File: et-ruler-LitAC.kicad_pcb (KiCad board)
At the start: 2 copper layers, 166 x 28 mm, 27 parts, among them J1 Conn_01x03, J2 AudioJack2, J3 Pmod-Interface-GPIO6, J4 Pmod-Interface-GPIO6, SW1 SW_DPDT, U1 OP07

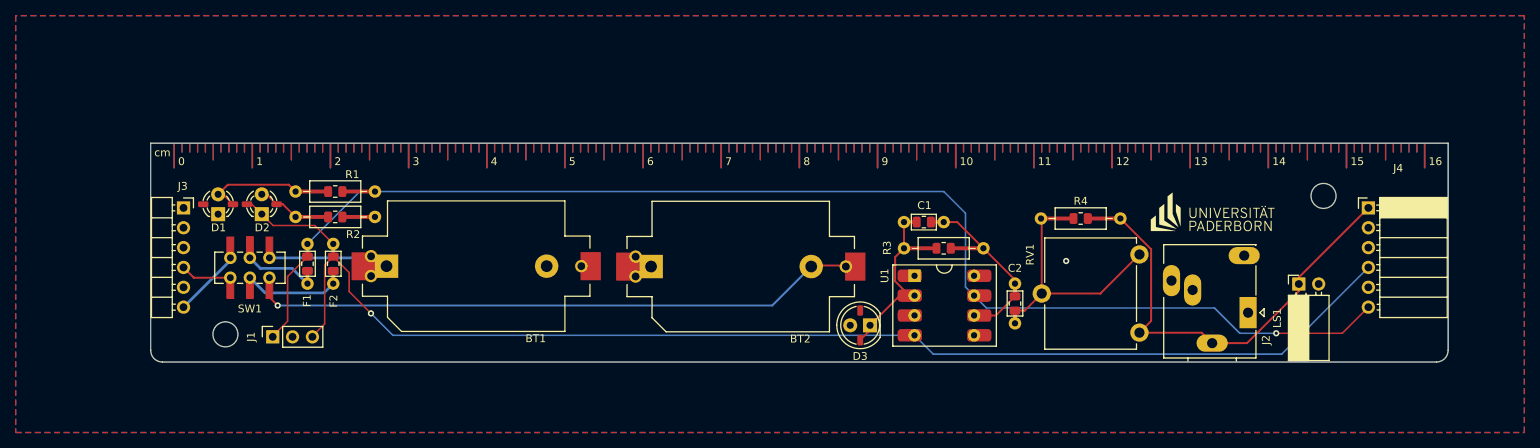
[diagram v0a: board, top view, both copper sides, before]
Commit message: Widen power tracks
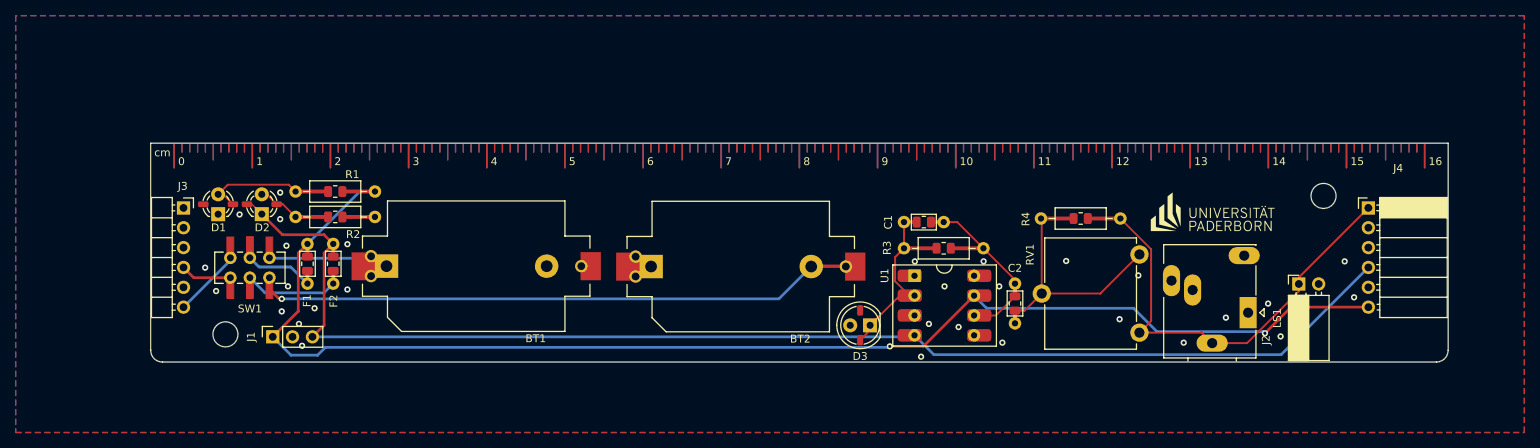
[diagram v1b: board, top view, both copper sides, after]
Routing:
- net V+: track 165.1 -> 175.4 mm, vias 1 -> 2
- net Net-(BT2--): track 78.0 -> 81.1 mm
- net Net-(BT1-+): track 14.6 -> 17.3 mm
- net V-: track 168.2 -> 169.3 mm, vias 1 -> 0
- net GND: vias 1 -> 30

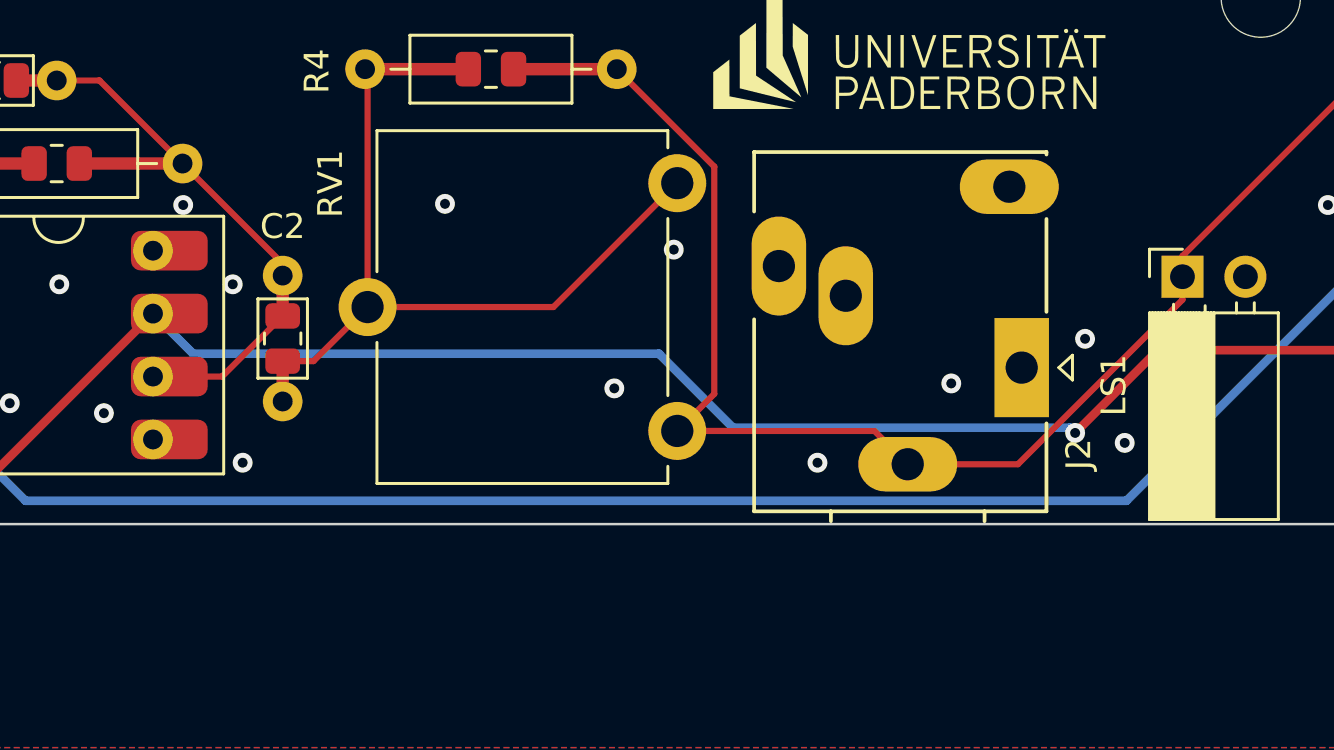
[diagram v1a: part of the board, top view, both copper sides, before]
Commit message: Use correct audio jack
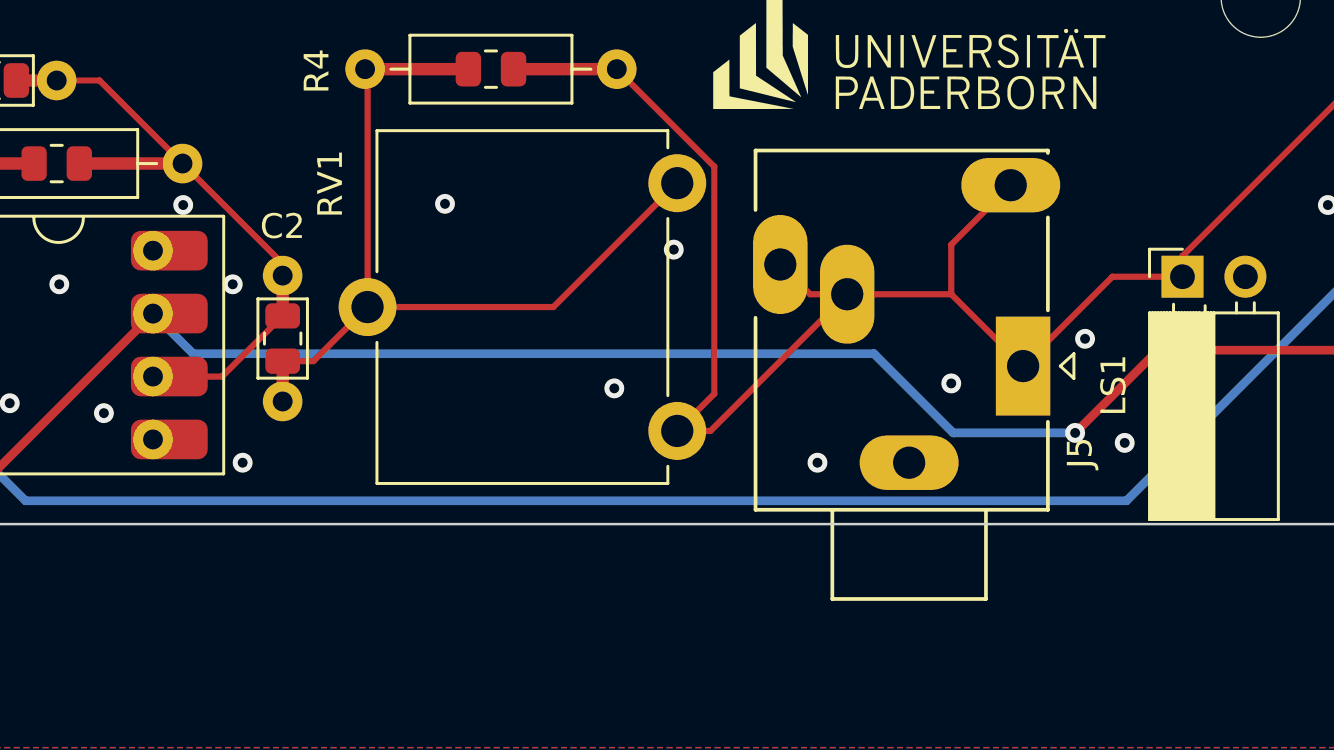
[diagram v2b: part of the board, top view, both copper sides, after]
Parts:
- removed J2: AudioJack2, Connector_Audio:Jack_3.5mm_Ledino_KB3SPRS_Horizontal
- added J5: AudioJack3_SwitchTR, Connector_Audio:Jack_3.5mm_Ledino_KB3SPRS_Horizontal, F.Cu at (189.5, 82.9)
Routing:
- net amp_out: track 54.9 -> 64.2 mm

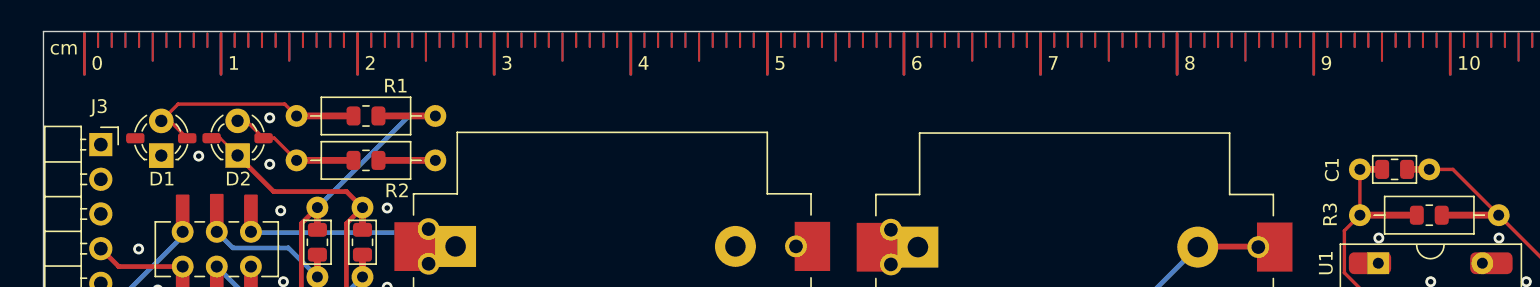
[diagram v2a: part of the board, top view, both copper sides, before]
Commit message: Use pmod footprints from correct library
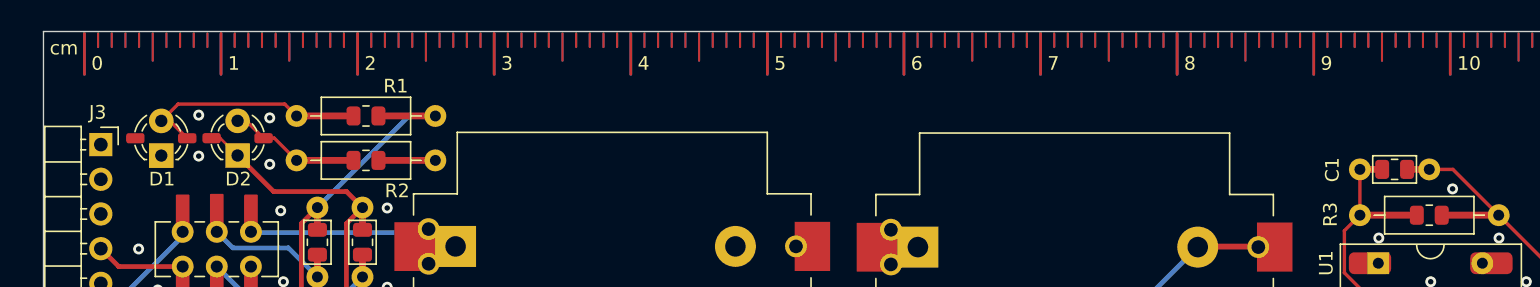
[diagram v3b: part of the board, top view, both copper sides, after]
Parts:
- J3: footprint emt-pmod:Pmod_Interface_Male6 -> Pmod_Interface-emt:Pmod_Interface_Male6
- J4: footprint emt-pmod:Pmod_Interface_Female6 -> Pmod_Interface-emt:Pmod_Interface_Female6
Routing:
- net GND: vias 30 -> 32
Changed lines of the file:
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@@
     (pad "" np_thru_hole circle (at 0 0) (size 3.2 3.2) (drill 3.2) (layers "F&B.Cu" "*.Mask"))
   )
-  (footprint "emt-pmod:Pmod_Interface_Male6" (layer "F.Cu")
+  (footprint "Pmod_Interface-emt:Pmod_Interface_Male6" (layer "F.Cu")
     (at 53.232 69.558)
     (descr "Through hole angled pin header, 1x06, 2.54mm pitch, 6mm pin length, single row")
@@
     (property "ki_keywords" "connector")
     (attr through_hole)
-    (fp_text reference "J3" (at -0.1 -2.78) (layer "F.SilkS")
+    (fp_text reference "J3" (at -0.232 -2.358) (layer "F.SilkS")
         (effects (font (size 1 1) (thickness 0.15)))
     )
-    (fp_text value "Pmod-Interface-GPIO6" (at -6.232 6.442 90) (layer "F.Fab")
+    (fp_text value "Pmod-Interface-GPIO6" (at -0.92 17.68) (layer "F.Fab")
         (effects (font (size 1 1) (thickness 0.15)))
     )
@@
     (fp_line (start 0.32 13.02) (end -1.5 13.02)
       (stroke (width 0.1) (type solid)) (layer "F.Fab"))
-    (pad "1" thru_hole rect (at 0 0) (size 1.7 1.7) (drill 1) (layers "F&B.Cu" "*.Mask")
+    (pad "1" thru_hole rect (at 0 0) (size 1.7 1.7) (drill 1) (layers "*.Cu" "*.Mask")
       (net 11 "unconnected-(J3-IO1-Pad1)") (pinfunction "IO1") (pintype "bidirectional+no_connect"))
-    (pad "2" thru_hole oval (at 0 2.54) (size 1.7 1.7) (drill 1) (layers "F&B.Cu" "*.Mask")
+    (pad "2" thru_hole oval (at 0 2.54) (size 1.7 1.7) (drill 1) (layers "*.Cu" "*.Mask")
       (net 15 "unconnected-(J3-IO2-Pad2)") (pinfunction "IO2") (pintype "bidirectional+no_connect"))
-    (pad "3" thru_hole oval (at 0 5.08) (size 1.7 1.7) (drill 1) (layers "F&B.Cu" "*.Mask")
+    (pad "3" thru_hole oval (at 0 5.08) (size 1.7 1.7) (drill 1) (layers "*.Cu" "*.Mask")
       (net 16 "unconnected-(J3-IO3-Pad3)") (pinfunction "IO3") (pintype "bidirectional+no_connect"))
-    (pad "4" thru_hole oval (at 0 7.62) (size 1.7 1.7) (drill 1) (layers "F&B.Cu" "*.Mask")
+    (pad "4" thru_hole oval (at 0 7.62) (size 1.7 1.7) (drill 1) (layers "*.Cu" "*.Mask")
       (net 12 "V-_ext_in") (pinfunction "IO4") (pintype "bidirectional"))
-    (pad "5" thru_hole oval (at 0 10.16) (size 1.7 1.7) (drill 1) (layers "F&B.Cu" "*.Mask")
+    (pad "5" thru_hole oval (at 0 10.16) (size 1.7 1.7) (drill 1) (layers "*.Cu" "*.Mask")
       (net 2 "GND") (pinfunction "GND") (pintype "power_in"))
-    (pad "6" thru_hole oval (at 0 12.7) (size 1.7 1.7) (drill 1) (layers "F&B.Cu" "*.Mask")
+    (pad "6" thru_hole oval (at 0 12.7) (size 1.7 1.7) (drill 1) (layers "*.Cu" "*.Mask")
       (net 13 "V+_ext_in") (pinfunction "VCC") (pintype "power_in"))
     (model "${KICAD6_3DMODEL_DIR}/Connector_PinHeader_2.54mm.3dshapes/PinHeader_1x06_P2.54mm_Horizontal.wrl"
@@
     )
   )
-  (footprint "emt-pmod:Pmod_Interface_Female6" (layer "F.Cu")
+  (footprint "Pmod_Interface-emt:Pmod_Interface_Female6" (layer "F.Cu")
     (at 204.832 69.558)
     (descr "Through hole angled socket strip, 1x06, 2.54mm pitch, 8.51mm socket length, single row (from Kicad 4.0.7), script generated")
@@
         (effects (font (size 1 1) (thickness 0.15)))
     )
-    (fp_text value "Pmod-Interface-GPIO6" (at 12.168 6.442 -90) (layer "F.Fab")
+    (fp_text value "Pmod-Interface-GPIO6" (at 4.92 17.53 180) (layer "F.Fab")
         (effects (font (size 1 1) (thickness 0.15)))
     )
@@
   (via (at 175.4 78.2) (size 0.8) (drill 0.4) (layers "F.Cu" "B.Cu") (free) (net 2))
   (via (at 158 86.8) (size 0.8) (drill 0.4) (layers "F.Cu" "B.Cu") (free) (net 2))
+  (via (at 60.4 67.4) (size 0.8) (drill 0.4) (layers "F.Cu" "B.Cu") (free) (net 2))
   (via (at 147.6 88.6) (size 0.8) (drill 0.4) (layers "F.Cu" "B.Cu") (free) (net 2))
   (via (at 157.6 79.6) (size 0.8) (drill 0.4) (layers "F.Cu" "B.Cu") (free) (net 2))
@@
   (via (at 65.6 67.6) (size 0.8) (drill 0.4) (layers "F.Cu" "B.Cu") (free) (net 2))
   (via (at 181.2 86.8) (size 0.8) (drill 0.4) (layers "F.Cu" "B.Cu") (free) (net 2))
+  (via (at 152.2 72.8) (size 0.8) (drill 0.4) (layers "F.Cu" "B.Cu") (free) (net 2))
   (via (at 201.8 76.4) (size 0.8) (drill 0.4) (layers "F.Cu" "B.Cu") (free) (net 2))
   (segment (start 133.5207 76.935) (end 137.9537 76.935) (width 0.25) (layer "F.Cu") (net 3))

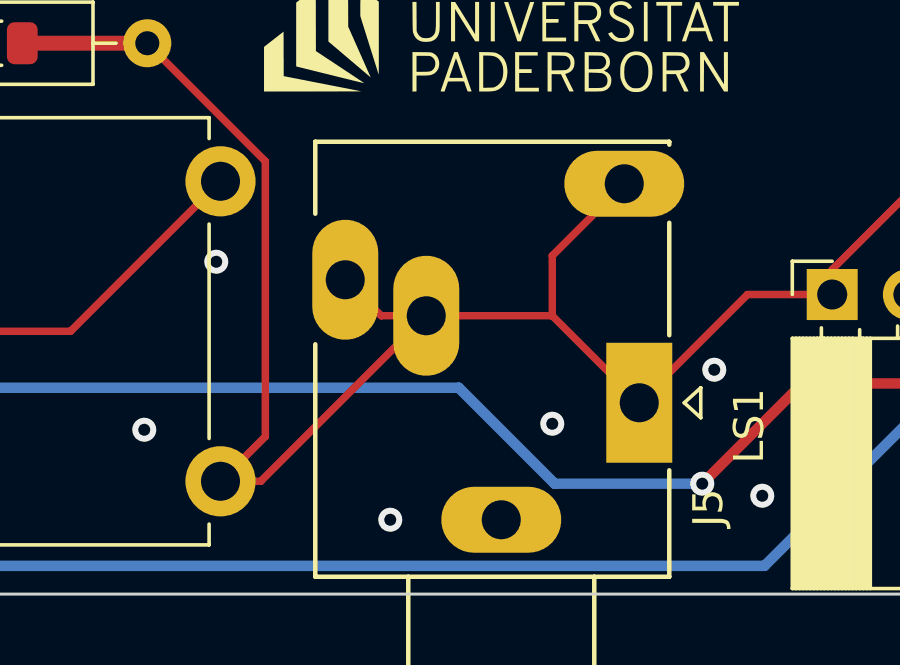
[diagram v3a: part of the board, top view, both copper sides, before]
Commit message: Only connect tip/left channel of audio jack
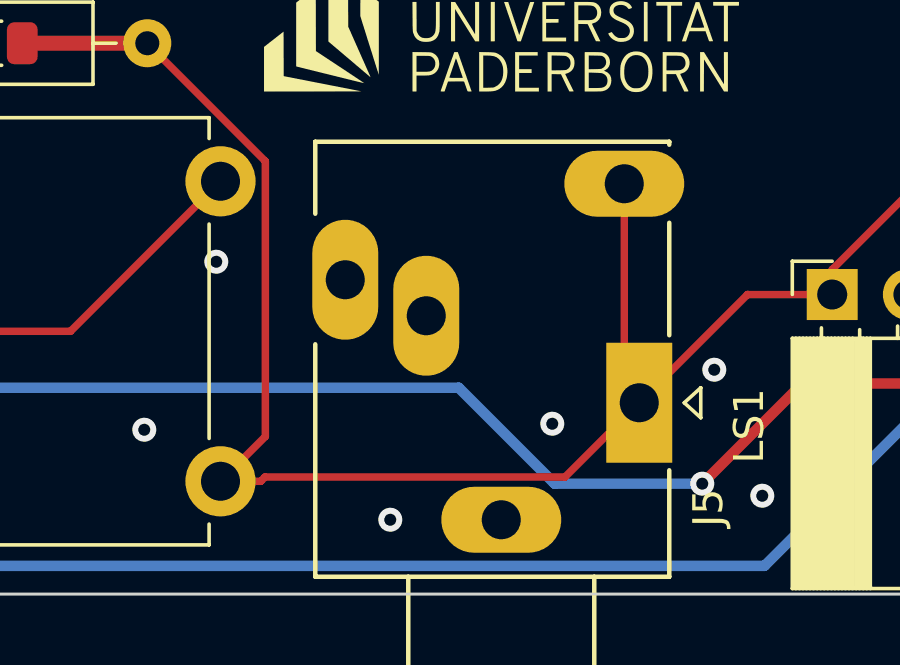
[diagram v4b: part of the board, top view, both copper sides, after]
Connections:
- J5 pad R: amp_out -> unconnected-(J5-PadR)
- J5 pad RN: amp_out -> unconnected-(J5-PadRN)
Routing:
- net amp_out: track 64.2 -> 60.7 mm
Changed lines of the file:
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@@
   (net 22 "unconnected-(U1-VOS-Pad8)")
   (net 23 "Net-(C2-Pad2)")
+  (net 24 "unconnected-(J5-PadR)")
+  (net 25 "unconnected-(J5-PadRN)")
   (footprint "et-ruler-footprints:Metric_Ruler_160mm_top" (layer "F.Cu")
     (at 52.032 61.4172)
@@
       (stroke (width 0.12) (type solid)) (fill none) (layer "F.Fab"))
     (pad "R" thru_hole oval (at 4.1 -9.8 90) (size 4 2.2) (drill 1.3) (layers "*.Cu" "*.Mask")
-      (net 14 "amp_out") (pintype "passive"))
+      (net 24 "unconnected-(J5-PadR)") (pintype "passive+no_connect"))
     (pad "RN" thru_hole oval (at 2.9 -7.1 90) (size 4 2.2) (drill 1.3) (layers "*.Cu" "*.Mask")
-      (net 14 "amp_out") (pintype "passive"))
+      (net 25 "unconnected-(J5-PadRN)") (pintype "passive+no_connect"))
     (pad "S" thru_hole oval (at -3.9 -4.6 90) (size 2.2 4) (drill 1.3) (layers "*.Cu" "*.Mask")
       (net 2 "GND") (pintype "passive"))
@@
   (segment (start 53.232 82.258) (end 59.222 76.268) (width 0.35) (layer "B.Cu") (net 13))
   (segment (start 59.222 76.268) (end 59.222 75.946) (width 0.35) (layer "B.Cu") (net 13))
-  (segment (start 189 75.6) (end 186.6 78) (width 0.25) (layer "F.Cu") (net 14))
+  (segment (start 189 75.6) (end 189 82.4) (width 0.25) (layer "F.Cu") (net 14))
   (segment (start 189.5 82.9) (end 193.107 79.293) (width 0.25) (layer "F.Cu") (net 14))
-  (segment (start 179.7 78.8) (end 180.9 80) (width 0.25) (layer "F.Cu") (net 14))
   (segment (start 173.101 70.916) (end 177.036 74.851) (width 0.25) (layer "F.Cu") (net 14))
-  (segment (start 176.882 85.518) (end 182.4 80) (width 0.25) (layer "F.Cu") (net 14))
-  (segment (start 182.4 80) (end 186.6 80) (width 0.25) (layer "F.Cu") (net 14))
-  (segment (start 180.9 80) (end 182.4 80) (width 0.25) (layer "F.Cu") (net 14))
+  (segment (start 189 82.4) (end 189.5 82.9) (width 0.25) (layer "F.Cu") (net 14))
   (segment (start 177.036 74.851) (end 177.036 84.023) (width 0.25) (layer "F.Cu") (net 14))
-  (segment (start 186.6 80) (end 189.5 82.9) (width 0.25) (layer "F.Cu") (net 14))
   (segment (start 175.541 85.518) (end 176.882 85.518) (width 0.25) (layer "F.Cu") (net 14))
   (segment (start 177.036 84.023) (end 175.541 85.518) (width 0.25) (layer "F.Cu") (net 14))
+  (segment (start 177.025 85.375) (end 187.025 85.375) (width 0.25) (layer "F.Cu") (net 14))
+  (segment (start 176.882 85.518) (end 177.025 85.375) (width 0.25) (layer "F.Cu") (net 14))
   (segment (start 195.931 79.293) (end 195.931 78.459) (width 0.25) (layer "F.Cu") (net 14))
+  (segment (start 187.025 85.375) (end 189.5 82.9) (width 0.25) (layer "F.Cu") (net 14))
   (segment (start 193.107 79.293) (end 195.931 79.293) (width 0.25) (layer "F.Cu") (net 14))
-  (segment (start 186.6 78) (end 186.6 80) (width 0.25) (layer "F.Cu") (net 14))
   (segment (start 195.931 78.459) (end 204.832 69.558) (width 0.25) (layer "F.Cu") (net 14))
   (segment (start 155.0419 83.322) (end 157.169 83.322) (width 0.25) (layer "F.Cu") (net 19))
